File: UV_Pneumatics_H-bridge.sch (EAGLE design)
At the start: 13 parts, among them IC1 74LS06N

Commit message: Updated schematic with Author and Version data
No substantive changes
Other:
- note added: "1.0"
- note added: "Author: Charles B. Malloch, PhD"
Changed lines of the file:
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@@
 2 - up / ~down
 1 - enable</text>
+<text x="142.24" y="7.62" size="2.54" layer="94" font="vector">Author: Charles B. Malloch, PhD</text>
+<text x="231.14" y="-12.7" size="2.54" layer="94" font="vector">1.0</text>
 </plain>
 <instances>

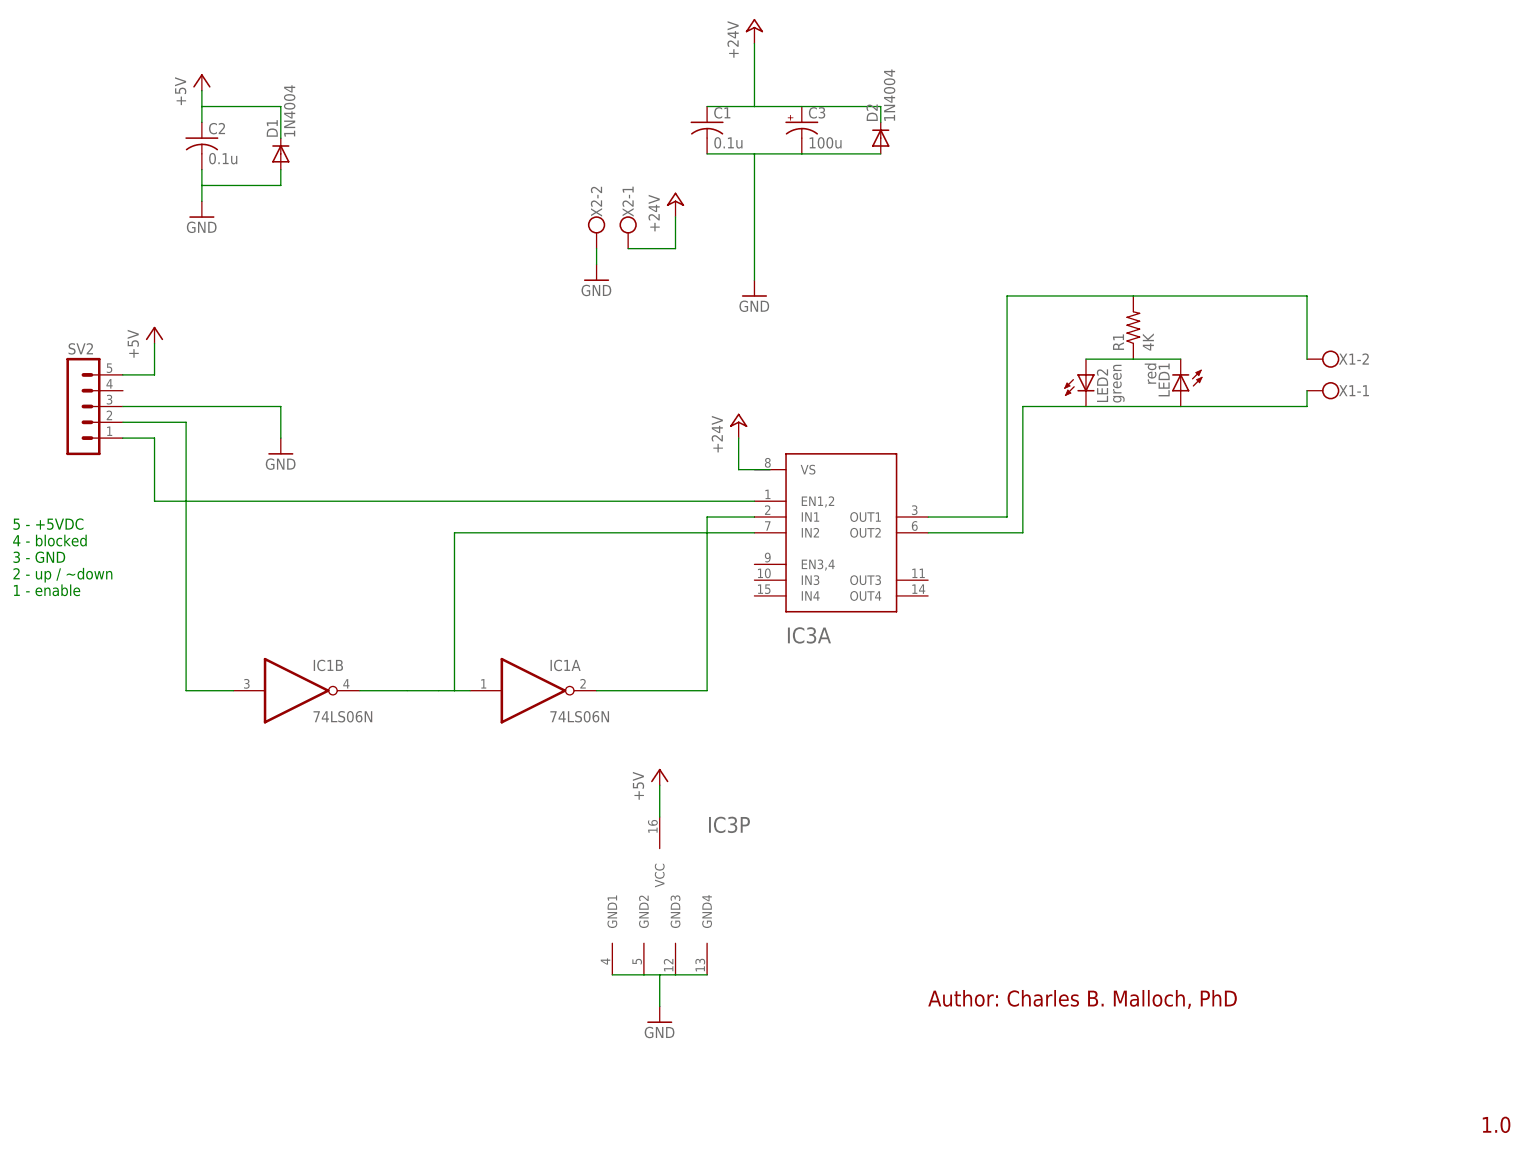
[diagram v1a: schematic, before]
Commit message: V2.0
As built. Replaced 74LS06 with 74LS04, which is TTL as intended
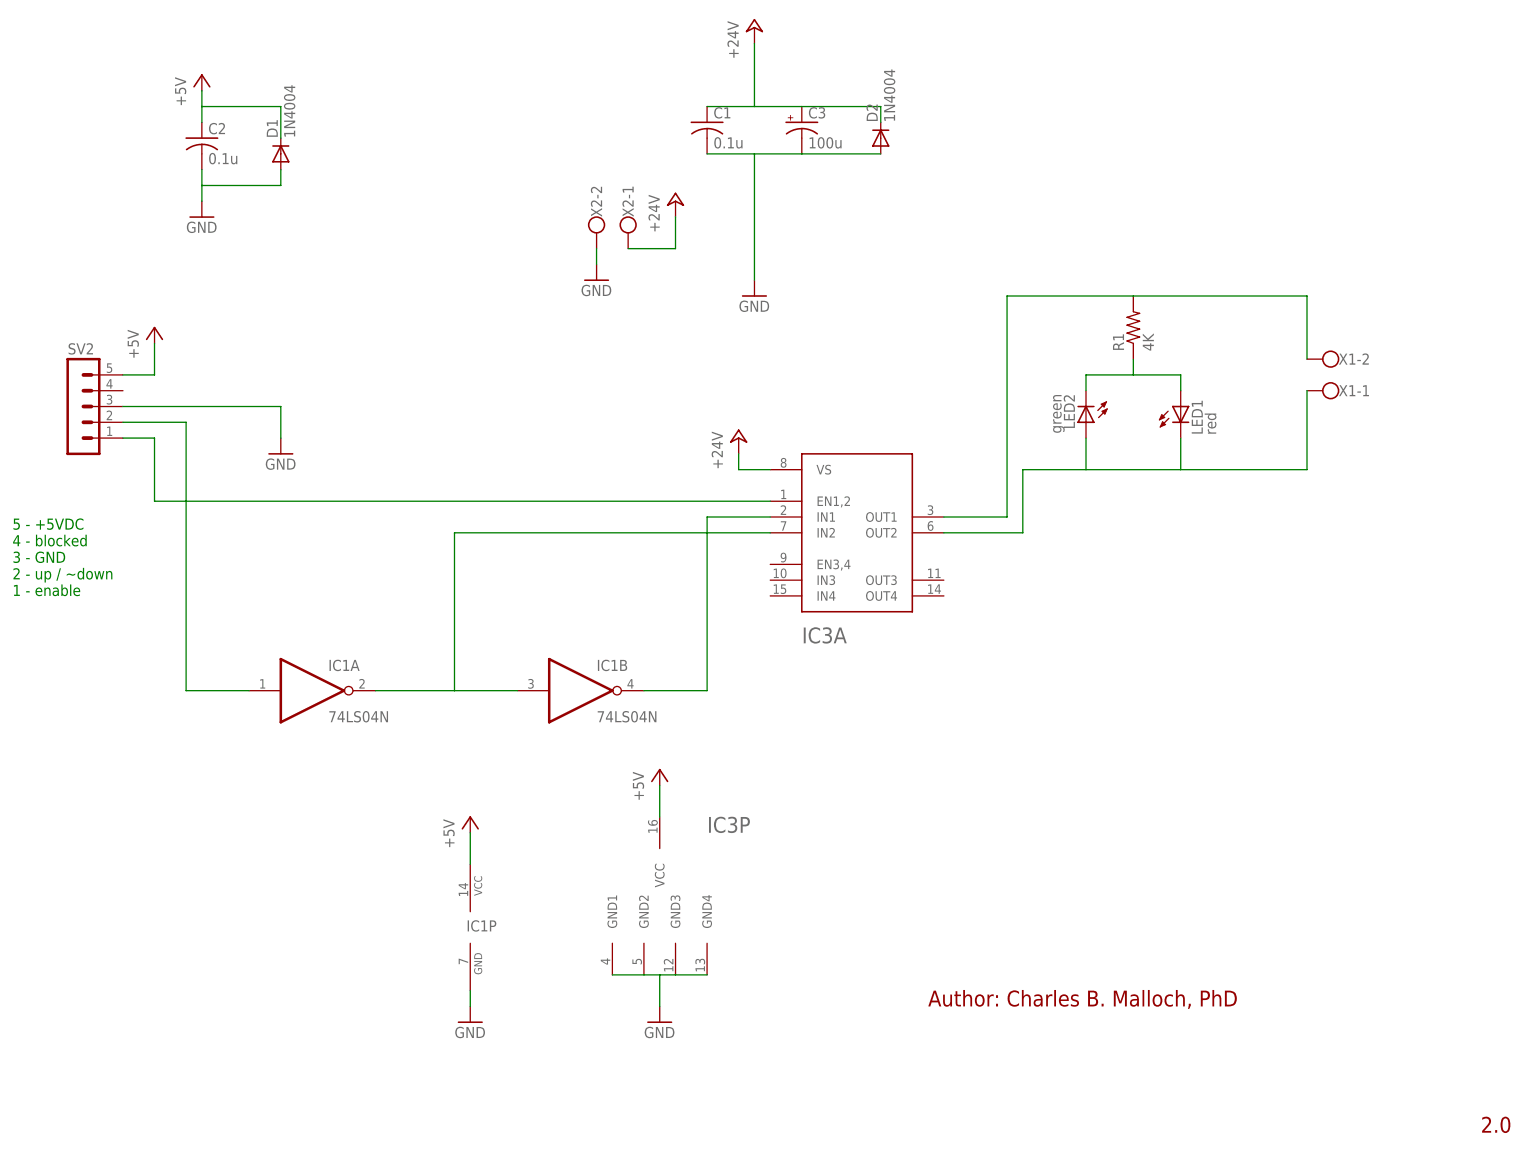
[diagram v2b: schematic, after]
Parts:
- IC1: value 74LS06N -> 74LS04N; device 74xx-us:74LS06N -> 74xx-us:74LS04N
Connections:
- removed net N$8: LED1.C, LED2.A, R1.1
- new net N$5: LED1.A, LED2.C, R1.1
- net +24V: now also IC3A.VS
- net +5V: now also IC1P.VCC
- net GND: now also IC1P.GND
- net N$1: now also IC1A.I; no longer IC1B.I
- net N$2: now also IC1A.O, IC1B.I; no longer IC1A.I, IC1B.O
- net N$3: now also IC1B.O; no longer IC1A.O
- net N$7: now also LED1.C, LED2.A; no longer LED1.A, LED2.C
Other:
- note added: "2.0"
- note removed: "1.0"
- moved on the sheet: IC1A, IC1B, IC3A, LED1, LED2
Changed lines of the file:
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@@
 </classes>
 <parts>
-<part name="IC1" library="74xx-us" deviceset="74*06" device="N" technology="LS"/>
+<part name="IC1" library="74xx-us" deviceset="74*04" device="N" technology="LS"/>
 <part name="IC3" library="ads" deviceset="L293D" device=""/>
 <part name="R1" library="resistor" deviceset="R-US_" device="0207/10" value="4K"/>
@@
 <part name="D1" library="diode" deviceset="1N4004" device=""/>
 <part name="D2" library="diode" deviceset="1N4004" device=""/>
+<part name="P+7" library="supply1" deviceset="+5V" device=""/>
+<part name="GND1" library="supply1" deviceset="GND" device=""/>
 </parts>
 <sheets>
@@
 1 - enable</text>
 <text x="142.24" y="7.62" size="2.54" layer="94" font="vector">Author: Charles B. Malloch, PhD</text>
-<text x="231.14" y="-12.7" size="2.54" layer="94" font="vector">1.0</text>
+<text x="231.14" y="-12.7" size="2.54" layer="94" font="vector">2.0</text>
 </plain>
 <instances>
-<instance part="IC1" gate="A" x="78.74" y="58.42"/>
-<instance part="IC1" gate="B" x="40.64" y="58.42"/>
-<instance part="IC3" gate="A" x="121.92" y="73.66"/>
+<instance part="IC1" gate="A" x="43.18" y="58.42"/>
+<instance part="IC1" gate="B" x="86.36" y="58.42"/>
+<instance part="IC3" gate="A" x="124.46" y="73.66"/>
 <instance part="IC3" gate="P" x="99.06" y="25.4"/>
 <instance part="R1" gate="G$1" x="175.26" y="116.84" rot="R90"/>
-<instance part="LED1" gate="G$1" x="182.88" y="106.68" rot="R180"/>
+<instance part="LED1" gate="G$1" x="182.88" y="104.14"/>
 <instance part="X1" gate="-1" x="208.28" y="106.68" rot="R180"/>
 <instance part="X1" gate="-2" x="208.28" y="111.76" rot="R180"/>
@@
 <instance part="C2" gate="G$1" x="25.4" y="147.32"/>
 <instance part="C3" gate="G$1" x="121.92" y="149.86"/>
-<instance part="LED2" gate="G$1" x="167.64" y="109.22"/>
-<instance part="P+1" gate="1" x="111.76" y="101.6"/>
+<instance part="LED2" gate="G$1" x="167.64" y="101.6" rot="R180"/>
+<instance part="P+1" gate="1" x="111.76" y="99.06"/>
 <instance part="P+2" gate="1" x="17.78" y="116.84"/>
 <instance part="GND2" gate="1" x="114.3" y="121.92"/>
@@
 <instance part="D1" gate="1" x="38.1" y="144.78" rot="R90"/>
 <instance part="D2" gate="1" x="134.62" y="147.32" rot="R90"/>
+<instance part="IC1" gate="P" x="68.58" y="20.32"/>
+<instance part="P+7" gate="1" x="68.58" y="38.1"/>
+<instance part="GND1" gate="1" x="68.58" y="5.08"/>
 </instances>
 <busses>
@@
 <pinref part="IC3" gate="P" pin="VCC"/>
 <wire x1="99.06" y1="43.18" x2="99.06" y2="38.1" width="0.1524" layer="91"/>
+</segment>
+<segment>
+<pinref part="IC1" gate="P" pin="VCC"/>
+<pinref part="P+7" gate="1" pin="+5V"/>
+<wire x1="68.58" y1="30.48" x2="68.58" y2="35.56" width="0.1524" layer="91"/>
 </segment>
 </net>
@@
 <wire x1="99.06" y1="7.62" x2="99.06" y2="12.7" width="0.1524" layer="91"/>
 </segment>
+<segment>
+<pinref part="GND1" gate="1" pin="GND"/>
+<pinref part="IC1" gate="P" pin="GND"/>
+<wire x1="68.58" y1="7.62" x2="68.58" y2="10.16" width="0.1524" layer="91"/>
+</segment>
 </net>
 <net name="N$1" class="0">
@@
 <wire x1="12.7" y1="101.6" x2="22.86" y2="101.6" width="0.1524" layer="91"/>
 <wire x1="22.86" y1="101.6" x2="22.86" y2="58.42" width="0.1524" layer="91"/>
-<pinref part="IC1" gate="B" pin="I"/>
-<wire x1="22.86" y1="58.42" x2="30.48" y2="58.42" width="0.1524" layer="91"/>
+<pinref part="IC1" gate="A" pin="I"/>
+<wire x1="22.86" y1="58.42" x2="33.02" y2="58.42" width="0.1524" layer="91"/>
 </segment>
 </net>
 <net name="N$2" class="0">
 <segment>
-<pinref part="IC1" gate="B" pin="O"/>
-<wire x1="50.8" y1="58.42" x2="58.42" y2="58.42" width="0.1524" layer="91"/>
-<wire x1="66.04" y1="58.42" x2="63.5" y2="58.42" width="0.1524" layer="91"/>
-<wire x1="58.42" y1="58.42" x2="63.5" y2="58.42" width="0.1524" layer="91"/>
-<pinref part="IC1" gate="A" pin="I"/>
-<wire x1="66.04" y1="58.42" x2="68.58" y2="58.42" width="0.1524" layer="91"/>
 <wire x1="66.04" y1="58.42" x2="66.04" y2="83.82" width="0.1524" layer="91"/>
 <pinref part="IC3" gate="A" pin="IN2"/>
-<wire x1="66.04" y1="83.82" x2="114.3" y2="83.82" width="0.1524" layer="91"/>
+<wire x1="66.04" y1="83.82" x2="116.84" y2="83.82" width="0.1524" layer="91"/>
+<pinref part="IC1" gate="A" pin="O"/>
+<wire x1="53.34" y1="58.42" x2="66.04" y2="58.42" width="0.1524" layer="91"/>
+<pinref part="IC1" gate="B" pin="I"/>
+<wire x1="66.04" y1="58.42" x2="76.2" y2="58.42" width="0.1524" layer="91"/>
 </segment>
 </net>
 <net name="N$3" class="0">
 <segment>
-<pinref part="IC1" gate="A" pin="O"/>
-<wire x1="88.9" y1="58.42" x2="106.68" y2="58.42" width="0.1524" layer="91"/>
 <wire x1="106.68" y1="58.42" x2="106.68" y2="86.36" width="0.1524" layer="91"/>
 <pinref part="IC3" gate="A" pin="IN1"/>
-<wire x1="106.68" y1="86.36" x2="114.3" y2="86.36" width="0.1524" layer="91"/>
+<wire x1="106.68" y1="86.36" x2="116.84" y2="86.36" width="0.1524" layer="91"/>
+<pinref part="IC1" gate="B" pin="O"/>
+<wire x1="96.52" y1="58.42" x2="106.68" y2="58.42" width="0.1524" layer="91"/>
 </segment>
 </net>
@@
 <wire x1="17.78" y1="99.06" x2="17.78" y2="88.9" width="0.1524" layer="91"/>
 <pinref part="IC3" gate="A" pin="EN1,2"/>
-<wire x1="17.78" y1="88.9" x2="114.3" y2="88.9" width="0.1524" layer="91"/>
+<wire x1="17.78" y1="88.9" x2="116.84" y2="88.9" width="0.1524" layer="91"/>
 </segment>
 </net>
@@
 <segment>
 <pinref part="P+1" gate="1" pin="+24V"/>
-<wire x1="111.76" y1="99.06" x2="111.76" y2="93.98" width="0.1524" layer="91"/>
+<wire x1="111.76" y1="96.52" x2="111.76" y2="93.98" width="0.1524" layer="91"/>
 <wire x1="111.76" y1="93.98" x2="116.84" y2="93.98" width="0.1524" layer="91"/>
+<pinref part="IC3" gate="A" pin="VS"/>
 </segment>
 </net>
@@
 <segment>
 <pinref part="IC3" gate="A" pin="OUT1"/>
-<wire x1="142.24" y1="86.36" x2="154.94" y2="86.36" width="0.1524" layer="91"/>
+<wire x1="144.78" y1="86.36" x2="154.94" y2="86.36" width="0.1524" layer="91"/>
 <wire x1="154.94" y1="86.36" x2="154.94" y2="121.92" width="0.1524" layer="91"/>
 <pinref part="R1" gate="G$1" pin="2"/>
@@
 <segment>
 <pinref part="IC3" gate="A" pin="OUT2"/>
-<wire x1="142.24" y1="83.82" x2="157.48" y2="83.82" width="0.1524" layer="91"/>
-<wire x1="157.48" y1="83.82" x2="157.48" y2="104.14" width="0.1524" layer="91"/>
+<wire x1="144.78" y1="83.82" x2="157.48" y2="83.82" width="0.1524" layer="91"/>
+<wire x1="157.48" y1="83.82" x2="157.48" y2="93.98" width="0.1524" layer="91"/>
+<pinref part="X1" gate="-1" pin="KL"/>
+<wire x1="157.48" y1="93.98" x2="167.64" y2="93.98" width="0.1524" layer="91"/>
+<wire x1="167.64" y1="93.98" x2="182.88" y2="93.98" width="0.1524" layer="91"/>
+<wire x1="182.88" y1="93.98" x2="203.2" y2="93.98" width="0.1524" layer="91"/>
+<wire x1="203.2" y1="93.98" x2="203.2" y2="106.68" width="0.1524" layer="91"/>
+<pinref part="LED2" gate="G$1" pin="A"/>
+<wire x1="167.64" y1="99.06" x2="167.64" y2="93.98" width="0.1524" layer="91"/>
+<pinref part="LED1" gate="G$1" pin="C"/>
+<wire x1="182.88" y1="99.06" x2="182.88" y2="93.98" width="0.1524" layer="91"/>
+</segment>
+</net>
+<net name="N$5" class="0">
+<segment>
+<pinref part="R1" gate="G$1" pin="1"/>
+<wire x1="175.26" y1="111.76" x2="175.26" y2="109.22" width="0.1524" layer="91"/>
+<wire x1="175.26" y1="109.22" x2="182.88" y2="109.22" width="0.1524" layer="91"/>
+<pinref part="LED1" gate="G$1" pin="A"/>
+<wire x1="182.88" y1="109.22" x2="182.88" y2="106.68" width="0.1524" layer="91"/>
 <pinref part="LED2" gate="G$1" pin="C"/>
-<wire x1="157.48" y1="104.14" x2="167.64" y2="104.14" width="0.1524" layer="91"/>
-<pinref part="LED1" gate="G$1" pin="A"/>
-<wire x1="167.64" y1="104.14" x2="182.88" y2="104.14" width="0.1524" layer="91"/>
-<pinref part="X1" gate="-1" pin="KL"/>
-<wire x1="182.88" y1="104.14" x2="203.2" y2="104.14" width="0.1524" layer="91"/>
-<wire x1="203.2" y1="104.14" x2="203.2" y2="106.68" width="0.1524" layer="91"/>
-</segment>
-</net>
-<net name="N$8" class="0">
-<segment>
-<pinref part="LED2" gate="G$1" pin="A"/>
-<pinref part="R1" gate="G$1" pin="1"/>
-<wire x1="167.64" y1="111.76" x2="175.26" y2="111.76" width="0.1524" layer="91"/>
-<pinref part="LED1" gate="G$1" pin="C"/>
-<wire x1="175.26" y1="111.76" x2="182.88" y2="111.76" width="0.1524" layer="91"/>
-</segment>
-</net>
+<wire x1="167.64" y1="106.68" x2="167.64" y2="109.22" width="0.1524" layer="91"/>
+<wire x1="167.64" y1="109.22" x2="175.26" y2="109.22" width="0.1524" layer="91"/>
+</segment>
+</net>
